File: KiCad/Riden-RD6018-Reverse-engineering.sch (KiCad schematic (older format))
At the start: 23 parts, among them Q0 Q_NMOS_GDS, Q3 Q_NMOS_GDS, T2 L_Core_Ferrite_Coupled

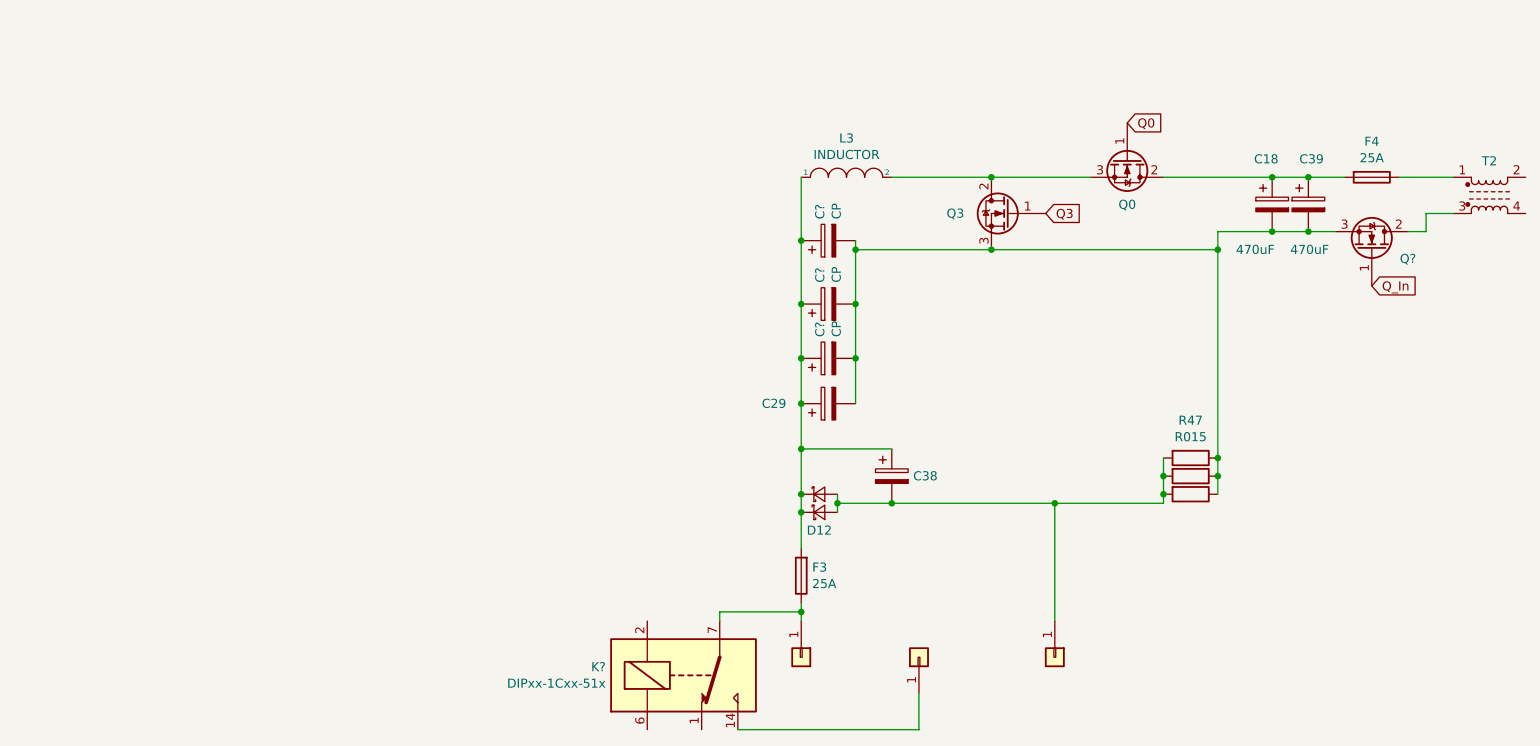
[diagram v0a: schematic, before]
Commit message: Ajout Pilotage Q0
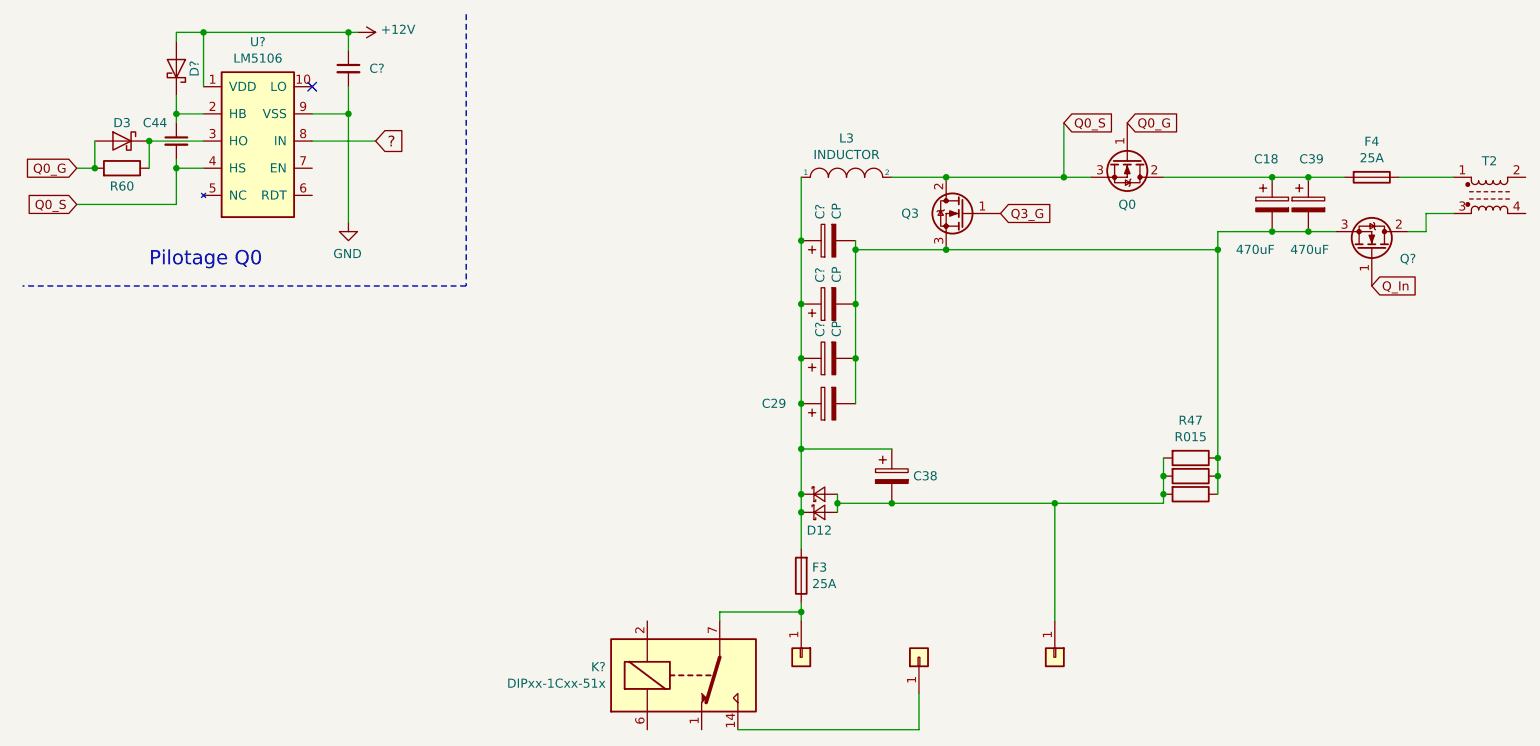
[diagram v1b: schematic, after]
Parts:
- added C44, C?: C_Small, symbol Device:C_Small
- added D3, D?: D_Schottky, symbol Device:D_Schottky
- added R60: R, symbol Device:R
- added U?: LM5106, symbol lm5106:LM5106
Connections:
- net Q0_S: now reaches L3.2, Q0.3 (S), Q3.2 (D)
- net Q0_S: now also C44.2, U?.4 (HS)
- net Q0 renamed Q0_G
- net Q0_G: now also D3.2 (A), R60.2
- net Q3 renamed Q3_G
- new net: D3.1 (K), R60.1, U?.3 (HO)
- new net: C44.1, D?.1 (K), U?.2 (HB)
- new net +12V: C?.1, D?.2 (A), U?.1 (VDD)
- new net ?: U?.8 (IN)
- new net GND: C?.2, U?.9 (VSS)
- no-connect marks 0 -> 1
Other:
- note added: "Pilotage Q0"
- moved on the sheet: Q3
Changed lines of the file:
@@
 L Device:Q_NMOS_GDS Q3
 U 1 1 5FDC3FB5
-P 6150 1750
-F 0 "Q3" H 6400 1750 50  0000 L CNN
-F 1 "Q_NMOS_GDS" H 6100 2100 50  0001 L CNN
-F 2 "" H 6350 1850 50  0001 C CNN
-F 3 "~" H 6150 1750 50  0001 C CNN
-	1    6150 1750
+P 5900 1750
+F 0 "Q3" H 6150 1750 50  0000 L CNN
+F 1 "Q_NMOS_GDS" H 5850 2100 50  0001 L CNN
+F 2 "" H 6100 1850 50  0001 C CNN
+F 3 "~" H 5900 1750 50  0001 C CNN
+	1    5900 1750
 	-1   0    0    -1
 $EndComp
@@
 	7800 1550 7600 1550
 Connection ~ 7800 1550
-Wire Wire Line
-	7600 1550 7000 1550
 Connection ~ 7600 1550
 Wire Wire Line
@@
 Connection ~ 7800 1850
 Wire Wire Line
-	6600 1550 6050 1550
+	6600 1550 6450 1550
 Connection ~ 5000 1900
 Wire Wire Line
@@
 	5300 2800 5300 2550
 Connection ~ 5300 2550
-Connection ~ 6050 1550
-Wire Wire Line
-	6050 1550 5500 1550
-Wire Wire Line
-	6050 1950 7300 1950
 Connection ~ 7300 1950
 Wire Wire Line
 	7300 1950 7300 3100
-Wire Wire Line
-	6050 1950 5300 1950
-Connection ~ 6050 1950
 Connection ~ 5300 1950
 Wire Wire Line
@@
 	4650 4600 5650 4600
 Text GLabel 6800 1250 2    50   Input ~ 0
-Q0
-Text GLabel 6350 1750 2    50   Input ~ 0
-Q3
+Q0_G
+Text GLabel 6100 1750 2    50   Input ~ 0
+Q3_G
 Text GLabel 8150 2150 2    50   Input ~ 0
 Q_In
+$Comp
+L Device:D_Schottky D3
+U 1 1 5FDC834F
+P 1250 1350
+F 0 "D3" H 1250 1450 50  0000 C CNN
+F 1 "D_Schottky" H 1300 1150 50  0001 C CNN
+F 2 "" H 1250 1350 50  0001 C CNN
+F 3 "~" H 1250 1350 50  0001 C CNN
+	1    1250 1350
+	-1   0    0    -1
+$EndComp
+$Comp
+L Device:R R60
+U 1 1 5FDC9AC7
+P 1250 1500
+F 0 "R60" V 1150 1500 50  0000 C CNN
+F 1 "R" H 1320 1455 50  0001 L CNN
+F 2 "" V 1180 1500 50  0001 C CNN
+F 3 "~" H 1250 1500 50  0001 C CNN
+	1    1250 1500
+	0    1    -1   0
+$EndComp
+Text GLabel 1000 1500 0    50   Input ~ 0
+Q0_G
+Wire Wire Line
+	1000 1500 1100 1500
+Text GLabel 6450 1250 2    50   Input ~ 0
+Q0_S
+Wire Wire Line
+	7000 1550 7600 1550
+Wire Wire Line
+	6450 1250 6450 1550
+Connection ~ 6450 1550
+Connection ~ 5800 1550
+Wire Wire Line
+	5800 1550 5500 1550
+Connection ~ 5800 1950
+Wire Wire Line
+	5800 1950 5300 1950
+Wire Wire Line
+	5800 1550 6450 1550
+Wire Wire Line
+	5800 1950 7300 1950
+$Comp
+L power:GND #PWR?
+U 1 1 5FDDAECA
+P 2500 1800
+F 0 "#PWR?" H 2500 1550 50  0001 C CNN
+F 1 "GND" H 2505 1627 50  0000 C CNN
+F 2 "" H 2500 1800 50  0001 C CNN
+F 3 "" H 2500 1800 50  0001 C CNN
+	1    2500 1800
+	-1   0    0    -1
+$EndComp
+Wire Wire Line
+	1100 1350 1100 1500
+Connection ~ 1100 1500
+Text GLabel 1000 1700 0    50   Input ~ 0
+Q0_S
+$Comp
+L Device:C_Small C?
+U 1 1 5FDEC5AB
+P 2500 950
+F 0 "C?" H 2300 950 50  0000 L CNN
+F 1 "C_Small" H 2592 905 50  0001 L CNN
+F 2 "" H 2500 950 50  0001 C CNN
+F 3 "~" H 2500 950 50  0001 C CNN
+	1    2500 950
+	-1   0    0    -1
+$EndComp
+$Comp
+L power:+12V #PWR?
+U 1 1 5FDEE2EF
+P 2550 750
+F 0 "#PWR?" H 2550 600 50  0001 C CNN
+F 1 "+12V" V 2565 878 50  0000 L CNN
+F 2 "" H 2550 750 50  0001 C CNN
+F 3 "" H 2550 750 50  0001 C CNN
+	1    2550 750
+	0    1    -1   0
+$EndComp
+Wire Wire Line
+	1550 1700 1000 1700
+Wire Wire Line
+	2500 1800 2500 1200
+Wire Wire Line
+	2550 750  2500 750
+$Comp
+L lm5106:LM5106 U?
+U 1 1 5FE0B631
+P 2000 850
+F 0 "U?" H 2000 897 50  0000 C CNN
+F 1 "LM5106" H 2000 806 50  0000 C CNN
+F 2 "" H 2000 850 50  0001 C CNN
+F 3 "" H 2000 850 50  0001 C CNN
+	1    2000 850
+	1    0    0    -1
+$EndComp
+Wire Wire Line
+	2500 750  2500 850
+Wire Wire Line
+	1700 1500 1550 1500
+Wire Wire Line
+	1550 1500 1550 1700
+Wire Wire Line
+	1400 1350 1400 1500
+Connection ~ 1400 1350
+Wire Wire Line
+	1400 1350 1700 1350
+Wire Wire Line
+	1550 1500 1550 1450
+Connection ~ 1550 1500
+Wire Wire Line
+	1550 1250 1550 1200
+Wire Wire Line
+	2300 1200 2500 1200
+Connection ~ 2500 1200
+Wire Wire Line
+	2500 1200 2500 1050
+Wire Wire Line
+	2300 1350 2650 1350
+Wire Wire Line
+	1700 1050 1700 750
+NoConn ~ 2300 1050
+$Comp
+L Device:C_Small C44
+U 1 1 5FDCA85B
+P 1550 1350
+F 0 "C44" H 1600 1450 50  0000 L CNN
+F 1 "C_Small" H 1642 1305 50  0001 L CNN
+F 2 "" H 1550 1350 50  0001 C CNN
+F 3 "~" H 1550 1350 50  0001 C CNN
+	1    1550 1350
+	-1   0    0    -1
+$EndComp
+Wire Wire Line
+	1700 1200 1550 1200
+Connection ~ 1550 1200
+Wire Wire Line
+	1550 1200 1550 1100
+$Comp
+L Device:D_Schottky D?
+U 1 1 5FDEC014
+P 1550 950
+F 0 "D?" H 1550 1050 50  0000 C CNN
+F 1 "D_Schottky" H 1600 750 50  0001 C CNN
+F 2 "" H 1550 950 50  0001 C CNN
+F 3 "~" H 1550 950 50  0001 C CNN
+	1    1550 950
+	0    1    -1   0
+$EndComp
+Wire Wire Line
+	1700 750  1550 750
+Wire Wire Line
+	1550 750  1550 800
+Wire Wire Line
+	1700 750  2500 750
+Connection ~ 1700 750
+Connection ~ 2500 750
+Text Notes 1400 2050 0    79   ~ 0
+Pilotage Q0
+Text GLabel 2650 1350 2    59   Input ~ 0
+?
+Wire Notes Line
+	3150 650  3150 2150
+Wire Notes Line
+	3150 2150 700  2150
 $EndSCHEMATC
